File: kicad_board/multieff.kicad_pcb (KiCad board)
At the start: 2 copper layers, 120 x 80 mm, 33 parts, among them J1 Wha1

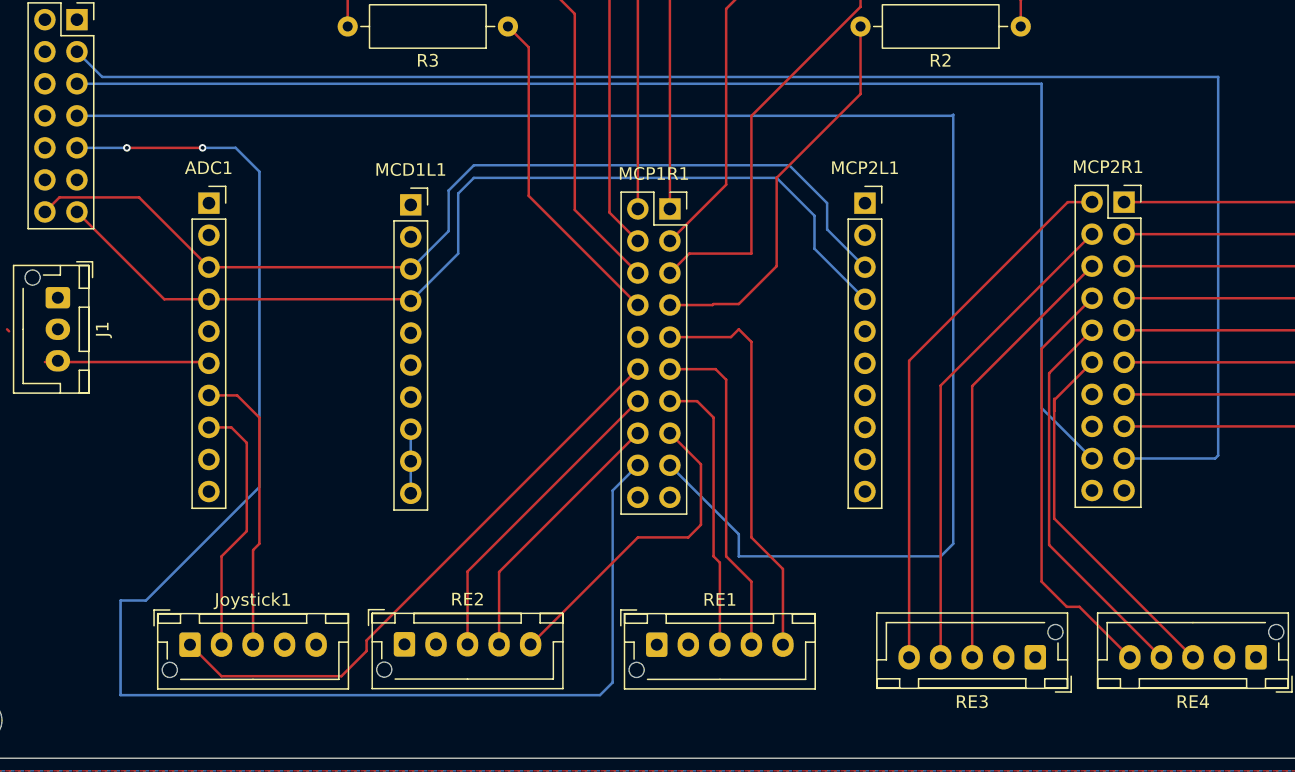
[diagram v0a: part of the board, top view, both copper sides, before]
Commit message: Correct traces geometry
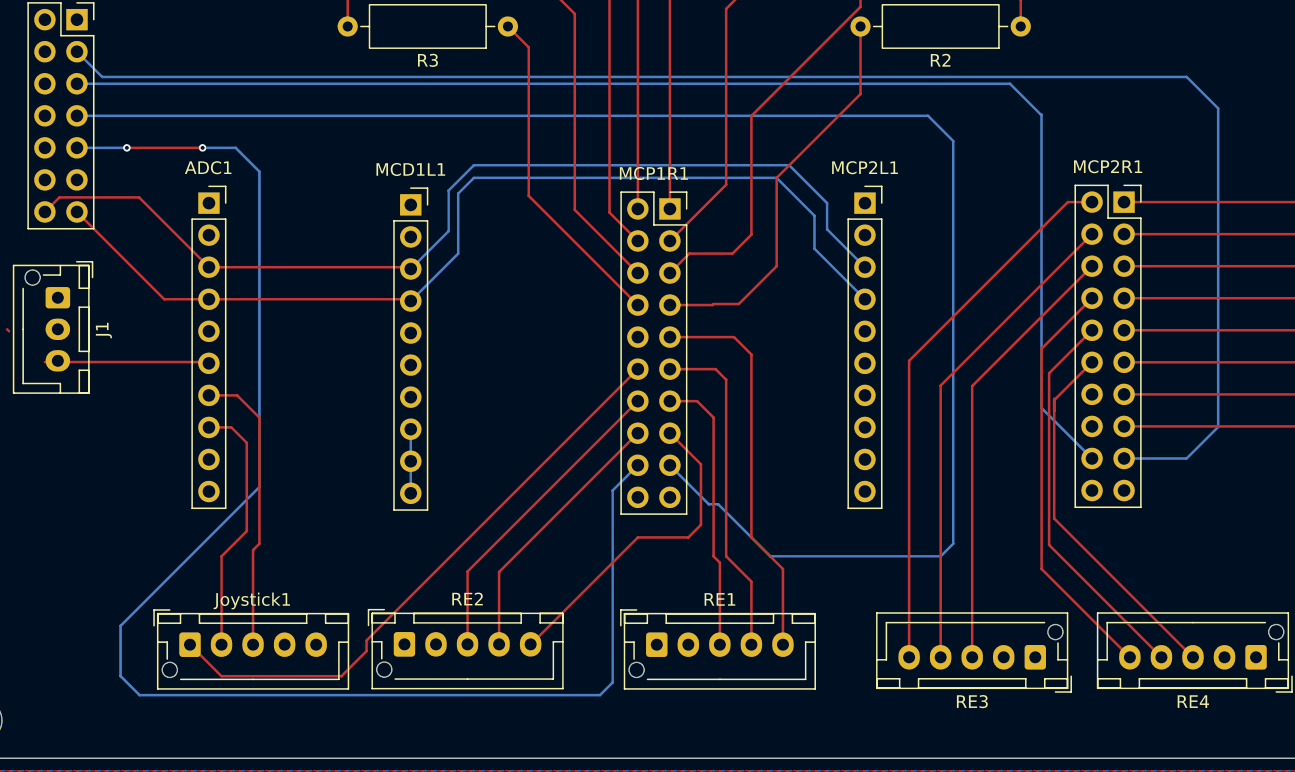
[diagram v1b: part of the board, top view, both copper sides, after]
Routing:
- net Net-(MCP2R1-Pin_17): track 128.8 -> 126.1 mm
- net Net-(MCP1R1-Pin_17): track 130.4 -> 128.1 mm
- net Net-(MCP1R1-Pin_18): track 119.9 -> 117.9 mm
- net Net-(MCP2R1-Pin_18): track 107.8 -> 106.4 mm
- net Net-(MCP1R1-Pin_9): track 32.2 -> 31.1 mm
- net Net-(MCP1R1-Pin_5): track 40.7 -> 39.8 mm
- net Net-(MCP2R1-Pin_8): track 33.6 -> 33.0 mm
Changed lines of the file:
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@@
 	(segment
 		(start 106 61.09295)
-		(end 106 72)
+		(end 106 70.5)
 		(width 0.2)
 		(layer "F.Cu")
@@
 	)
 	(segment
-		(start 106 72)
+		(start 104.5 72)
 		(end 101.08 72)
+		(width 0.2)
+		(layer "F.Cu")
+		(net 29)
+	)
+	(segment
+		(start 104.5 72)
+		(end 106 70.5)
 		(width 0.2)
 		(layer "F.Cu")
@@
 	)
 	(segment
+		(start 67 90.5)
+		(end 56 101.5)
+		(width 0.2)
+		(layer "B.Cu")
+		(net 34)
+	)
+	(segment
+		(start 95 90.78)
+		(end 97 88.78)
+		(width 0.2)
+		(layer "B.Cu")
+		(net 34)
+	)
+	(segment
+		(start 95 106)
+		(end 95 90.78)
+		(width 0.2)
+		(layer "B.Cu")
+		(net 34)
+	)
+	(segment
+		(start 56 101.5)
+		(end 56 105.5)
+		(width 0.2)
+		(layer "B.Cu")
+		(net 34)
+	)
+	(segment
+		(start 62.5 63.62)
+		(end 65.12 63.62)
+		(width 0.2)
+		(layer "B.Cu")
+		(net 34)
+	)
+	(segment
+		(start 67 65.5)
+		(end 67 90.5)
+		(width 0.2)
+		(layer "B.Cu")
+		(net 34)
+	)
+	(segment
 		(start 65.12 63.62)
-		(end 62.5 63.62)
-		(width 0.2)
-		(layer "B.Cu")
-		(net 34)
-	)
-	(segment
-		(start 67 65.5)
-		(end 65.12 63.62)
-		(width 0.2)
-		(layer "B.Cu")
-		(net 34)
-	)
-	(segment
-		(start 94 107)
-		(end 56 107)
-		(width 0.2)
-		(layer "B.Cu")
-		(net 34)
-	)
-	(segment
-		(start 95 90.78)
-		(end 95 106)
-		(width 0.2)
-		(layer "B.Cu")
-		(net 34)
-	)
-	(segment
-		(start 56 107)
-		(end 56 99.5)
-		(width 0.2)
-		(layer "B.Cu")
-		(net 34)
-	)
-	(segment
-		(start 58 99.5)
-		(end 67 90.5)
-		(width 0.2)
-		(layer "B.Cu")
-		(net 34)
-	)
-	(segment
-		(start 95 106)
-		(end 94 107)
-		(width 0.2)
-		(layer "B.Cu")
-		(net 34)
-	)
-	(segment
-		(start 56 99.5)
-		(end 58 99.5)
-		(width 0.2)
-		(layer "B.Cu")
-		(net 34)
-	)
-	(segment
-		(start 97 88.78)
-		(end 95 90.78)
+		(end 67 65.5)
 		(width 0.2)
 		(layer "B.Cu")
@@
 	)
 	(segment
-		(start 67 90.5)
-		(end 67 65.5)
+		(start 57.5 107)
+		(end 56 105.5)
+		(width 0.2)
+		(layer "B.Cu")
+		(net 34)
+	)
+	(segment
+		(start 94 107)
+		(end 95 106)
+		(width 0.2)
+		(layer "B.Cu")
+		(net 34)
+	)
+	(segment
+		(start 57.5 107)
+		(end 94 107)
 		(width 0.2)
 		(layer "B.Cu")
@@
 	(segment
 		(start 121 96)
-		(end 105 96)
-		(width 0.2)
-		(layer "B.Cu")
-		(net 36)
-	)
-	(segment
-		(start 122 61)
 		(end 122 95)
 		(width 0.2)
@@
 	)
 	(segment
-		(start 52.54 61.08)
-		(end 121.92 61.08)
-		(width 0.2)
-		(layer "B.Cu")
-		(net 36)
-	)
-	(segment
-		(start 105 96)
-		(end 105 94.24)
+		(start 120 61.08)
+		(end 52.54 61.08)
+		(width 0.2)
+		(layer "B.Cu")
+		(net 36)
+	)
+	(segment
+		(start 102.63 91.87)
+		(end 103.37 91.87)
 		(width 0.2)
 		(layer "B.Cu")
@@
 	(segment
 		(start 122 95)
+		(end 122 63.08)
+		(width 0.2)
+		(layer "B.Cu")
+		(net 36)
+	)
+	(segment
+		(start 122 63.08)
+		(end 120 61.08)
+		(width 0.2)
+		(layer "B.Cu")
+		(net 36)
+	)
+	(segment
+		(start 107.5 96)
 		(end 121 96)
 		(width 0.2)
@@
 	)
 	(segment
-		(start 105 94.24)
-		(end 99.54 88.78)
-		(width 0.2)
-		(layer "B.Cu")
-		(net 36)
-	)
-	(segment
-		(start 121.92 61.08)
-		(end 122 61)
+		(start 99.54 88.78)
+		(end 102.63 91.87)
+		(width 0.2)
+		(layer "B.Cu")
+		(net 36)
+	)
+	(segment
+		(start 103.37 91.87)
+		(end 107.5 96)
 		(width 0.2)
 		(layer "B.Cu")
@@
 	)
 	(segment
-		(start 129 58.54)
+		(start 129 61)
 		(end 129 84.24)
+		(width 0.2)
+		(layer "B.Cu")
+		(net 42)
+	)
+	(segment
+		(start 128.96 61)
+		(end 126.5 58.54)
 		(width 0.2)
 		(layer "B.Cu")
@@
 	(segment
 		(start 52.54 58.54)
-		(end 129 58.54)
+		(end 126.5 58.54)
 		(width 0.2)
 		(layer "B.Cu")
@@
 	)
 	(segment
-		(start 135.54 88.24)
-		(end 142.76 88.24)
-		(width 0.2)
-		(layer "B.Cu")
-		(net 45)
-	)
-	(segment
-		(start 143 88)
-		(end 143 58)
-		(width 0.2)
-		(layer "B.Cu")
-		(net 45)
+		(start 129 61)
+		(end 128.96 61)
+		(width 0.2)
+		(layer "B.Cu")
+		(net 42)
 	)
 	(segment
@@
 	)
 	(segment
-		(start 142.76 88.24)
-		(end 143 88)
+		(start 140.5 88.24)
+		(end 143 85.74)
 		(width 0.2)
 		(layer "B.Cu")
@@
 	)
 	(segment
-		(start 143 58)
+		(start 143 85.74)
+		(end 143 60.5)
+		(width 0.2)
+		(layer "B.Cu")
+		(net 45)
+	)
+	(segment
+		(start 140.5 58)
 		(end 54.54 58)
+		(width 0.2)
+		(layer "B.Cu")
+		(net 45)
+	)
+	(segment
+		(start 135.54 88.24)
+		(end 140.5 88.24)
+		(width 0.2)
+		(layer "B.Cu")
+		(net 45)
+	)
+	(segment
+		(start 143 60.5)
+		(end 140.5 58)
 		(width 0.2)
 		(layer "B.Cu")
@@
 	)
 	(segment
+		(start 136 104)
+		(end 129 97)
+		(width 0.2)
+		(layer "F.Cu")
+		(net 57)
+	)
+	(segment
+		(start 129 97)
+		(end 129 79.54)
+		(width 0.2)
+		(layer "F.Cu")
+		(net 57)
+	)
+	(segment
 		(start 129 79.54)
-		(end 129 98)
-		(width 0.2)
-		(layer "F.Cu")
-		(net 57)
-	)
-	(segment
-		(start 133 75.54)
-		(end 129 79.54)
-		(width 0.2)
-		(layer "F.Cu")
-		(net 57)
-	)
-	(segment
-		(start 129 98)
-		(end 131 100)
-		(width 0.2)
-		(layer "F.Cu")
-		(net 57)
-	)
-	(segment
-		(start 131 100)
-		(end 132 100)
-		(width 0.2)
-		(layer "F.Cu")
-		(net 57)
-	)
-	(segment
-		(start 132 100)
-		(end 136 104)
+		(end 133 75.54)
 		(width 0.2)
 		(layer "F.Cu")
@@
 	)
 	(segment
+		(start 99.54 78.62)
+		(end 104.62 78.62)
+		(width 0.2)
+		(layer "F.Cu")
+		(net 65)
+	)
+	(segment
+		(start 104.62 78.62)
+		(end 106 80)
+		(width 0.2)
+		(layer "F.Cu")
+		(net 65)
+	)
+	(segment
+		(start 106 80)
+		(end 106 94.5)
+		(width 0.2)
+		(layer "F.Cu")
+		(net 65)
+	)
+	(segment
 		(start 108.5 97)
 		(end 108.5 103)
 		(width 0.2)
 		(layer "F.Cu")
-		(net 65)
-	)
-	(segment
-		(start 106 79)
-		(end 106 94.5)
-		(width 0.2)
-		(layer "F.Cu")
-		(net 65)
-	)
-	(segment
-		(start 104.38 78.62)
-		(end 105 78)
-		(width 0.2)
-		(layer "F.Cu")
-		(net 65)
-	)
-	(segment
-		(start 99.54 78.62)
-		(end 104.38 78.62)
-		(width 0.2)
-		(layer "F.Cu")
-		(net 65)
-	)
-	(segment
-		(start 105 78)
-		(end 106 79)
-		(width 0.2)
-		(layer "F.Cu")

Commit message: Improve connectors placement
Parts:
- removed RE1, RE2, RE3, RE4: Conn_01x05, Connector_JST:JST_XH_B5B-XH-AM_1x05_P2.50mm_Vertical
- added RotaryEncoder1: Conn_01x05, Connector_JST:JST_XH_B5B-XH-AM_1x05_P2.50mm_Vertical, F.Cu at (93.4, 104.0)
- added RotaryEncoder2: Conn_01x05, Connector_JST:JST_XH_B5B-XH-AM_1x05_P2.50mm_Vertical, F.Cu at (110.9, 104.0)
- added RotaryEncoder3: Conn_01x05, Connector_JST:JST_XH_B5B-XH-AM_1x05_P2.50mm_Vertical, F.Cu at (128.5, 104.0)
- added RotaryEncoder4: Conn_01x05, Connector_JST:JST_XH_B5B-XH-AM_1x05_P2.50mm_Vertical, F.Cu at (146.0, 104.0)
- moved Joystick1 13.5 mm to (75.0, 104.0), turned to 180 degrees
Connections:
- Joystick1 pad 1: Net-(Joystick1-Pin_1) -> GND
- Joystick1 pad 2: Net-(ADC1-Pin_8) -> +3.3V
- Joystick1 pad 3: Net-(ADC1-Pin_7) -> Net-(Joystick1-Pin_3)
- Joystick1 pad 4: +3.3V -> Net-(ADC1-Pin_7)
- Joystick1 pad 5: GND -> Net-(ADC1-Pin_8)
- MCP1R1 pad 12: Net-(Joystick1-Pin_1) -> Net-(Joystick1-Pin_3)
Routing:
- net Net-(Joystick1-Pin_1): track 47.1 -> 0.00 mm
- net Net-(MCP1R1-Pin_18): track 117.9 -> 72.1 mm
- net Net-(Joystick1-Pin_3): track 0.00 -> 36.5 mm
- net Net-(MCP1R1-Pin_13): track 22.2 -> 23.9 mm
- net Net-(ADC1-Pin_8): track 20.3 -> 19.0 mm
- net Net-(MCP2R1-Pin_12): track 30.2 -> 29.2 mm
- net Net-(ADC1-Pin_7): track 22.9 -> 23.9 mm
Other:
- board text removed: "CJMCU-2317"

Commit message: Ongoing work
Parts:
- removed MCD1L1, MCP2L1: Conn_01x10, Connector_PinSocket_2.54mm:PinSocket_1x10_P2.54mm_Vertical
- removed MCP1R1, MCP2R1: Conn_02x10_Odd_Even, Connector_PinSocket_2.54mm:PinSocket_2x10_P2.54mm_Vertical
- removed the R1 at (127.3, 42.0)
- removed the R2 at (127.3, 54.0)
- removed the R3 at (86.7, 54.0)
- added ?: , buzzardLabel, F.Cu at (105.0, 2.85)
- added ?: , buzzardLabel, F.Cu at (110.0, 21.4)
- added ?: , buzzardLabel, F.Cu at (107.6, 2.85)
- added ?: , buzzardLabel, F.Cu at (97.4, 25.6)
- added ?: , buzzardLabel, F.Cu at (103.5, 12.4)
- added ?: , buzzardLabel, F.Cu at (110.0, 6.75)
- added ?: , buzzardLabel, F.Cu at (101.5, 16.6)
- added ?: , buzzardLabel, F.Cu at (100.0, 25.6)
- added ?: , buzzardLabel, F.Cu at (107.6, 25.6)
- added ?: , buzzardLabel, B.Cu at (95.5, 14.2)
- added ?: , buzzardLabel, B.Cu at (93.0, 14.2)
- added ?: , buzzardLabel, F.Cu at (102.5, 25.6)
- added ?: , buzzardLabel, B.Cu at (91.0, 14.2)
- added ?: , buzzardLabel, B.Cu at (103.0, 11.6)
- added ?: , buzzardLabel, F.Cu at (99.3, 16.6)
- added ?: , buzzardLabel, F.Cu at (105.0, 25.6)
- added ?: , buzzardLabel, F.Cu at (95.5, 18.1)
- added ?: , buzzardLabel, F.Cu at (97.4, 2.85)
- added ?: , buzzardLabel, F.Cu at (102.5, 2.85)
- added ?: , buzzardLabel, F.Cu at (100.0, 2.85)
- added ?: , buzzardLabel, F.Cu at (103.7, 16.6)
- added C1: 0.1uF, e-radionica.com footprinti:0603C, F.Cu at (98.5, 11.9)
- added C3: 1uF, PCM_Capacitor_SMD_AKL:C_1206_3216Metric, F.Cu at (124.0, 81.8)
- added C4: 1uF, PCM_Capacitor_SMD_AKL:C_1206_3216Metric, F.Cu at (97.8, 88.8)
- added FD1: FIDUCIAL, e-radionica.com footprinti:FIDUCIAL_23, F.Cu at (91.5, 14.2)
- added G***: LOGO, Soldered Graphics:Logo-Back-OSH-3.5mm, F.Cu at (98.7, 20.1)
- added G***: LOGO, Soldered Graphics:Logo-Front-easyC-5mm, F.Cu at (92.2, 9.85)
- added G***: LOGO, Soldered Graphics:Logo-Front-easyC-5mm, F.Cu at (108.8, 9.85)
- added G***: LOGO, Soldered Graphics:Logo-Front-Soldered-3mm, F.Cu at (92.5, 19.1)
- added G***: LOGO, Soldered Graphics:Symbol-Front-Voltmeter, B.Cu at (98.7, 8.45)
- added H1: HOLE_3.2mm, e-radionica.com footprinti:HOLE_3.2mm, F.Cu at (92.5, 6.25)
- added H2: HOLE_3.2mm, e-radionica.com footprinti:HOLE_3.2mm, F.Cu at (92.5, 22.2)
- added JP1: SMD_JUMPER_3_PAD_TRACE, e-radionica.com footprinti:SMD_JUMPER_3_PAD_TRACE, F.Cu at (103.5, 11.2)
- added JP2: 0x48, e-radionica.com footprinti:SMD_JUMPER_CONNECTED, F.Cu at (95.5, 19.2)
- added JP3: 0x49, e-radionica.com footprinti:SMD_JUMPER, F.Cu at (103.5, 17.8)
- added JP4: 0x4A, e-radionica.com footprinti:SMD_JUMPER, F.Cu at (101.5, 17.8)
- added JP5: 0x4B, e-radionica.com footprinti:SMD_JUMPER, F.Cu at (99.5, 17.8)
- added K1: HEADER_MALE_5X1, e-radionica.com footprinti:HEADER_MALE_5X1, B.Cu at (102.5, 5.36)
- added K2: HEADER_MALE_4X1, e-radionica.com footprinti:HEADER_MALE_4X1, B.Cu at (103.8, 23.1)
- added K3: easyC-SMD, e-radionica.com footprinti:easyC-connector, F.Cu at (92.8, 14.2)
- added K4: easyC-SMD, e-radionica.com footprinti:easyC-connector, F.Cu at (108.2, 14.2)
- added K5: HEADER_MALE_1X1, e-radionica.com footprinti:HEADER_MALE_1X1, B.Cu at (97.4, 23.1)
- added R1: 10k, e-radionica.com footprinti:0603R, F.Cu at (98.5, 10.6)
- added R1: 480, PCM_Resistor_SMD_AKL:R_1206_3216Metric_Pad1.30x1.75mm_HandSolder, F.Cu at (124.5, 38.0)
- added R2: 480, PCM_Resistor_SMD_AKL:R_1206_3216Metric_Pad1.30x1.75mm_HandSolder, F.Cu at (124.2, 47.5)
- added R2: 10k, e-radionica.com footprinti:0603R, F.Cu at (104.8, 9.85)
- added R3: 10k, e-radionica.com footprinti:0603R, F.Cu at (102.1, 9.85)
- added R3: 480, PCM_Resistor_SMD_AKL:R_1206_3216Metric_Pad1.30x1.75mm_HandSolder, F.Cu at (79.8, 46.5)
- added R6: 10k, PCM_Resistor_SMD_AKL:R_1206_3216Metric, F.Cu at (123.5, 91.0)
- added R7: 10k, PCM_Resistor_SMD_AKL:R_1206_3216Metric, F.Cu at (123.5, 87.8)
- added R8: 10k, PCM_Resistor_SMD_AKL:R_1206_3216Metric, F.Cu at (107.8, 90.0)
- added R9: 10k, PCM_Resistor_SMD_AKL:R_1206_3216Metric, F.Cu at (103.5, 90.0)
- added REF**: Logo-Front-SolderedFULL-13mm, Soldered Graphics:Logo-Back-SolderedFULL-13mm, F.Cu at (109.0, 14.2)
- added REF**: Version1.1.1., Soldered Graphics:Version1.1.1., B.Cu at (90.2, 23.2)
- added REF**: Symbol-Front-I2C-ADDR-Field, Soldered Graphics:Symbol-Front-I2C-ADDR-Field, B.Cu at (103.0, 14.2)
- added RN1: 10k, PCM_Resistor_SMD_AKL:R_Array_Convex_4x1206, F.Cu at (103.8, 69.0)
- added RN2: 10k, PCM_Resistor_SMD_AKL:R_Array_Convex_4x1206, F.Cu at (144.8, 87.5)
- added U1: MCP23017_SO, Package_SO:SOIC-28W_7.5x17.9mm_P1.27mm, F.Cu at (97.5, 79.9)
- added U1: ADS1115, e-radionica.com footprinti:VSSOP, F.Cu at (100.5, 14.2)
- added U2: MCP23017_SO, Package_SO:SOIC-28W_7.5x17.9mm_P1.27mm, F.Cu at (134.0, 81.0)
- C1: value C -> 1uF
- C2: value C_Polarized -> 100uF
- Pisound1: footprint Connector_PinSocket_2.54mm:PinSocket_2x07_P2.54mm_Vertical -> Connector_IDC:IDC-Header_2x07_P2.54mm_Vertical_SMD
- R4, R5: footprint Resistor_THT:R_Axial_DIN0309_L9.0mm_D3.2mm_P12.70mm_Horizontal -> PCM_Resistor_SMD_AKL:R_1206_3216Metric_Pad1.30x1.75mm_HandSolder
- moved RotaryEncoder4 63.3 mm to (82.8, 103.0), turned to 0 degrees
- moved RotaryEncoder1 51.4 mm to (144.8, 103.2)
- moved RotaryEncoder3 28.5 mm to (100.0, 102.8), turned to 0 degrees
- moved RotaryEncoder2 16.1 mm to (127.0, 103.2)
- moved Pisound1 13.4 mm to (52.2, 66.9)
- moved R4 10.7 mm to (79.8, 37.2)
- moved J1 10.0 mm to (51.0, 85.5)
- moved ADC1 3.89 mm to (63.0, 71.9)
- moved Joystick1 0.69 mm to (74.5, 103.5)
- moved R5 0.25 mm to (62.8, 37.5), turned to 0 degrees
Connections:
- Joystick1 pad 4: Net-(ADC1-Pin_7) -> Net-(ADC1-Pin_8)
- Joystick1 pad 5: Net-(ADC1-Pin_8) -> Net-(ADC1-Pin_7)
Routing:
- net Net-(Pisound1-Pin_7): track 128.1 -> 0.00 mm
- net Net-(Pisound1-Pin_3): track 126.1 -> 0.00 mm
- net Net-(Pisound1-Pin_5): track 106.4 -> 0.00 mm
- net /SDA: track 77.5 -> 0.00 mm
- net /SCL: track 77.5 -> 0.00 mm
- net Net-(Pisound1-Pin_9): track 72.1 -> 0.00 mm, vias 2 -> 0
- net Net-(RotaryEncoder3-Pin_5): track 43.2 -> 0.00 mm
- net VCC: track 0.00 -> 41.0 mm, vias 0 -> 1
- net Net-(MCP1R1-Pin_5): track 39.8 -> 0.00 mm
- net Net-(RotaryEncoder3-Pin_4): track 38.5 -> 0.00 mm
- net Net-(Joystick1-Pin_3): track 36.5 -> 0.00 mm
- net SCL: track 0.00 -> 35.8 mm, vias 0 -> 2
- net Net-(RotaryEncoder3-Pin_3): track 34.9 -> 0.00 mm
- net Net-(U1-GPA1): track 34.7 -> 0.00 mm
- net Net-(PB1-Pin_2): track 34.4 -> 0.42 mm
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- added copper zone on F.Cu, net +3.3V
- added copper zone on B.Cu, net GND
- removed copper zone on B.Cu, net +3.3V
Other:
- board size 120 x 80 mm -> 120 x 108.8 mm
- board text removed: "+5V / GND"
- board text removed: "A0"
- board text removed: "A1"
- board text removed: "A2"
- board text removed: "B0 / A0"
- board text removed: "B1 / A1"
- board text removed: "B2 / A2"
- board text removed: "B3 / A3"
- board text removed: "B4 / A4"
- board text removed: "B5 / A5"
- board text removed: "B6 / A6"
- board text removed: "B7 / A7"
- board text removed: "GND"
- board text removed: "ITB / ITA"
- board text removed: "MCP23017"
- board text removed: "NC / CS"
- board text removed: "NC / S0"
- board text removed: "RST"
- board text removed: "SCL / SCK"
- board text removed: "SDA / SI"
- board text removed: "VCC"

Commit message: Work in progress
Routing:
- net Net-(PB3-Pin_2): track 4.80 -> 0.64 mm
